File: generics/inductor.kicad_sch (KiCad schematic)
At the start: 1 part

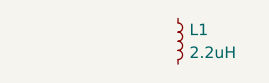
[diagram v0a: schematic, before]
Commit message: Add ESP32 and relevant peripherals
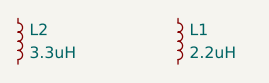
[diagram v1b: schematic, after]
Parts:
- added L2: 3.3uH, Custom_DCDC:SRU5028-3R3Y, symbol Device:L_Small
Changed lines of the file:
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@@
 			)
 		)
-		(property "Description" "Inductor, small symbol"
+		(property "Description" "CR 7A, Isat 8A, Shielded, 20%, 32mOhm"
 			(at 82.55 95.25 0)
 			(effects
@@
 		)
 		(instances
-			(project ""
+			(project "generics"
 				(path "/ff075d90-2677-48ca-91fd-a3a441ca4e63/4ade81d9-8575-4e61-ba1a-89956bff33f7"
 					(reference "L1")
 					(unit 1)
 				)
+			)
+		)
+	)
+	(symbol
+		(lib_id "Device:L_Small")
+		(at 64.77 95.25 0)
+		(unit 1)
+		(exclude_from_sim no)
+		(in_bom yes)
+		(on_board yes)
+		(dnp no)
+		(fields_autoplaced yes)
+		(property "Reference" "L2"
+			(at 66.04 93.9799 0)
+			(effects
+				(font
+					(size 1.27 1.27)
+				)
+				(justify left)
+			)
+		)
+		(property "Value" "3.3uH"
+			(at 66.04 96.5199 0)
+			(effects
+				(font
+					(size 1.27 1.27)
+				)
+				(justify left)
+			)
+		)
+		(property "Footprint" "Custom_DCDC:SRU5028-3R3Y"
+			(at 64.77 95.25 0)
+			(effects
+				(font
+					(size 1.27 1.27)
+				)
+				(hide yes)
+			)
+		)
+		(property "Datasheet" "~"
+			(at 64.77 95.25 0)
+			(effects
+				(font
+					(size 1.27 1.27)
+				)
+				(hide yes)
+			)
+		)
+		(property "Description" "CR 2.8A, Isat 2.1A, Shielded, 30%, 24mOhm"
+			(at 64.77 95.25 0)
+			(effects
+				(font
+					(size 1.27 1.27)
+				)
+				(hide yes)
+			)
+		)
+		(property "MPN" "SRU5028-3R3Y"
+			(at 64.77 95.25 0)
+			(effects
+				(font
+					(size 1.27 1.27)
+				)
+				(hide yes)
+			)
+		)
+		(property "Mfr" "Bourns Inc."
+			(at 64.77 95.25 0)
+			(effects
+				(font
+					(size 1.27 1.27)
+				)
+				(hide yes)
+			)
+		)
+		(pin "1"
+		)
+		(pin "2"
+		)
+		(instances
+			(project "generics"
+				(path "/ff075d90-2677-48ca-91fd-a3a441ca4e63/4ade81d9-8575-4e61-ba1a-89956bff33f7"
+					(reference "L2")
+					(unit 1)
+				)
